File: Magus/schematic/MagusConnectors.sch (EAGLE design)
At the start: 7 parts

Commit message: Magus Rev01 board
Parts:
- renumbered C28 to C1, D3 to D1, D4 to D2, JP13 to JP2, JP3 to JP1
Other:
- note added: "Copyright 2017 Rebel Technology"
- note added: "Published under the GNU GPL"
- note removed: "Copyright Rebel Technology 2017"
- note removed: "Published under the GNU GPL v2"
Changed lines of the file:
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@@
 <part name="GND158" library="supply1" deviceset="GND" device=""/>
 <part name="GND159" library="supply1" deviceset="GND" device=""/>
-<part name="JP13" library="jumper" deviceset="JP1Q" device=""/>
+<part name="JP2" library="jumper" deviceset="JP1Q" device=""/>
 <part name="GND163" library="supply1" deviceset="GND" device=""/>
-<part name="C28" library="Rebel" deviceset="C-EU" device="C1206" value="10u"/>
+<part name="C1" library="Rebel" deviceset="C-EU" device="C1206" value="10u"/>
 <part name="P+13" library="supply1" deviceset="+5V" device=""/>
 <part name="X1" library="con-usb-3" deviceset="USB" device="-A-H"/>
 <part name="X3" library="con-usb-3" deviceset="USB" device="-B-H"/>
-<part name="JP3" library="pinhead" deviceset="PINHD-2X4" device=""/>
+<part name="JP1" library="pinhead" deviceset="PINHD-2X4" device=""/>
 <part name="GND26" library="supply1" deviceset="GND" device=""/>
-<part name="D3" library="diode" deviceset="BAT54S" device=""/>
-<part name="D4" library="diode" deviceset="BAT54S" device=""/>
+<part name="D1" library="diode" deviceset="BAT54S" device=""/>
+<part name="D2" library="diode" deviceset="BAT54S" device=""/>
 <part name="P+1" library="supply1" deviceset="+5V" device=""/>
 <part name="GND1" library="supply1" deviceset="GND" device=""/>
@@
 <plain>
 <text x="5.08" y="119.38" size="3.048" layer="97" font="vector">Magus Rev01</text>
-<text x="5.08" y="114.3" size="3.048" layer="97" font="vector">Copyright Rebel Technology 2017</text>
-<text x="5.08" y="109.22" size="3.048" layer="97" font="vector">Published under the GNU GPL v2</text>
+<text x="5.08" y="114.3" size="3.048" layer="97" font="vector">Copyright 2017 Rebel Technology</text>
+<text x="5.08" y="109.22" size="3.048" layer="97" font="vector">Published under the GNU GPL</text>
 </plain>
 <instances>
 <instance part="GND158" gate="1" x="53.34" y="78.74"/>
 <instance part="GND159" gate="1" x="53.34" y="35.56"/>
-<instance part="JP13" gate="A" x="43.18" y="45.72" smashed="yes" rot="R270">
+<instance part="JP2" gate="A" x="43.18" y="45.72" smashed="yes" rot="R270">
 <attribute name="NAME" x="40.64" y="43.18" size="1.778" layer="95"/>
 <attribute name="VALUE" x="38.1" y="41.275" size="1.778" layer="96"/>
 </instance>
 <instance part="GND163" gate="1" x="25.4" y="78.74"/>
-<instance part="C28" gate="G$1" x="25.4" y="88.9"/>
+<instance part="C1" gate="G$1" x="25.4" y="88.9"/>
 <instance part="P+13" gate="1" x="22.86" y="7.62" smashed="yes">
 <attribute name="VALUE" x="20.32" y="7.62" size="1.778" layer="96"/>
@@
 <instance part="X1" gate="G$1" x="58.42" y="91.44"/>
 <instance part="X3" gate="G$1" x="58.42" y="43.18"/>
-<instance part="JP3" gate="A" x="35.56" y="10.16"/>
+<instance part="JP1" gate="A" x="35.56" y="10.16"/>
 <instance part="GND26" gate="1" x="48.26" y="2.54"/>
-<instance part="D3" gate="G$1" x="20.32" y="93.98" rot="MR90"/>
-<instance part="D4" gate="G$1" x="5.08" y="45.72" rot="MR90"/>
+<instance part="D1" gate="G$1" x="20.32" y="93.98" rot="MR90"/>
+<instance part="D2" gate="G$1" x="5.08" y="45.72" rot="MR90"/>
 <instance part="P+1" gate="1" x="20.32" y="104.14"/>
 <instance part="GND1" gate="1" x="20.32" y="78.74"/>
@@
 <segment>
 <wire x1="50.8" y1="45.72" x2="55.88" y2="45.72" width="0.1524" layer="91"/>
-<pinref part="JP13" gate="A" pin="2"/>
+<pinref part="JP2" gate="A" pin="2"/>
 <pinref part="X3" gate="G$1" pin="VBUS"/>
 </segment>
@@
 <wire x1="33.02" y1="10.16" x2="5.08" y2="10.16" width="0.1524" layer="91"/>
 <label x="5.08" y="10.16" size="1.778" layer="95"/>
-<pinref part="JP3" gate="A" pin="5"/>
+<pinref part="JP1" gate="A" pin="5"/>
 </segment>
 </net>
@@
 <wire x1="33.02" y1="12.7" x2="5.08" y2="12.7" width="0.1524" layer="91"/>
 <label x="5.08" y="12.7" size="1.778" layer="95"/>
-<pinref part="JP3" gate="A" pin="3"/>
+<pinref part="JP1" gate="A" pin="3"/>
 </segment>
 </net>
 <net name="EXT_USB_D_VBUS" class="0">
 <segment>
-<pinref part="JP13" gate="A" pin="1"/>
+<pinref part="JP2" gate="A" pin="1"/>
 <wire x1="35.56" y1="45.72" x2="7.62" y2="45.72" width="0.1524" layer="91"/>
 <label x="10.16" y="45.72" size="1.778" layer="95"/>
-<pinref part="D4" gate="G$1" pin="C1A2"/>
+<pinref part="D2" gate="G$1" pin="C1A2"/>
 </segment>
 <segment>
 <wire x1="33.02" y1="15.24" x2="5.08" y2="15.24" width="0.1524" layer="91"/>
 <label x="5.08" y="15.24" size="1.778" layer="95"/>
-<pinref part="JP3" gate="A" pin="1"/>
+<pinref part="JP1" gate="A" pin="1"/>
 </segment>
 </net>
@@
 <wire x1="25.4" y1="93.98" x2="22.86" y2="93.98" width="0.1524" layer="91"/>
 <wire x1="25.4" y1="91.44" x2="25.4" y2="93.98" width="0.1524" layer="91"/>
-<pinref part="C28" gate="G$1" pin="1"/>
+<pinref part="C1" gate="G$1" pin="1"/>
 <pinref part="X1" gate="G$1" pin="VBUS"/>
-<pinref part="D3" gate="G$1" pin="C1A2"/>
+<pinref part="D1" gate="G$1" pin="C1A2"/>
 <junction x="25.4" y="93.98"/>
 </segment>
@@
 <wire x1="66.04" y1="15.24" x2="40.64" y2="15.24" width="0.1524" layer="91"/>
 <label x="45.72" y="15.24" size="1.778" layer="95"/>
-<pinref part="JP3" gate="A" pin="2"/>
+<pinref part="JP1" gate="A" pin="2"/>
 </segment>
 </net>
@@
 <wire x1="66.04" y1="12.7" x2="40.64" y2="12.7" width="0.1524" layer="91"/>
 <label x="45.72" y="12.7" size="1.778" layer="95"/>
-<pinref part="JP3" gate="A" pin="4"/>
+<pinref part="JP1" gate="A" pin="4"/>
 </segment>
 </net>
@@
 <wire x1="66.04" y1="10.16" x2="40.64" y2="10.16" width="0.1524" layer="91"/>
 <label x="45.72" y="10.16" size="1.778" layer="95"/>
-<pinref part="JP3" gate="A" pin="6"/>
+<pinref part="JP1" gate="A" pin="6"/>
 </segment>
 </net>
 <net name="+5V" class="0">
 <segment>
-<pinref part="D3" gate="G$1" pin="C2"/>
+<pinref part="D1" gate="G$1" pin="C2"/>
 <pinref part="P+1" gate="1" pin="+5V"/>
 <wire x1="20.32" y1="101.6" x2="20.32" y2="99.06" width="0.1524" layer="91"/>
 </segment>
 <segment>
-<pinref part="D4" gate="G$1" pin="C2"/>
+<pinref part="D2" gate="G$1" pin="C2"/>
 <pinref part="P+2" gate="1" pin="+5V"/>
 <wire x1="5.08" y1="53.34" x2="5.08" y2="50.8" width="0.1524" layer="91"/>
@@
 <pinref part="P+13" gate="1" pin="+5V"/>
 <wire x1="22.86" y1="2.54" x2="22.86" y2="5.08" width="0.1524" layer="91"/>
-<pinref part="JP3" gate="A" pin="7"/>
+<pinref part="JP1" gate="A" pin="7"/>
 <wire x1="33.02" y1="7.62" x2="25.4" y2="7.62" width="0.1524" layer="91"/>
 <wire x1="25.4" y1="7.62" x2="25.4" y2="2.54" width="0.1524" layer="91"/>
@@
 <net name="GND" class="0">
 <segment>
-<pinref part="D3" gate="G$1" pin="A1"/>
+<pinref part="D1" gate="G$1" pin="A1"/>
 <pinref part="GND1" gate="1" pin="GND"/>
 <wire x1="20.32" y1="81.28" x2="20.32" y2="88.9" width="0.1524" layer="91"/>
 </segment>
 <segment>
-<pinref part="D4" gate="G$1" pin="A1"/>
+<pinref part="D2" gate="G$1" pin="A1"/>
 <pinref part="GND2" gate="1" pin="GND"/>
 <wire x1="5.08" y1="38.1" x2="5.08" y2="40.64" width="0.1524" layer="91"/>
@@
 <pinref part="GND163" gate="1" pin="GND"/>
 <wire x1="25.4" y1="81.28" x2="25.4" y2="83.82" width="0.1524" layer="91"/>
-<pinref part="C28" gate="G$1" pin="2"/>
+<pinref part="C1" gate="G$1" pin="2"/>
 </segment>
 <segment>
-<pinref part="JP3" gate="A" pin="8"/>
+<pinref part="JP1" gate="A" pin="8"/>
 <pinref part="GND26" gate="1" pin="GND"/>
 <wire x1="40.64" y1="7.62" x2="48.26" y2="7.62" width="0.1524" layer="91"/>

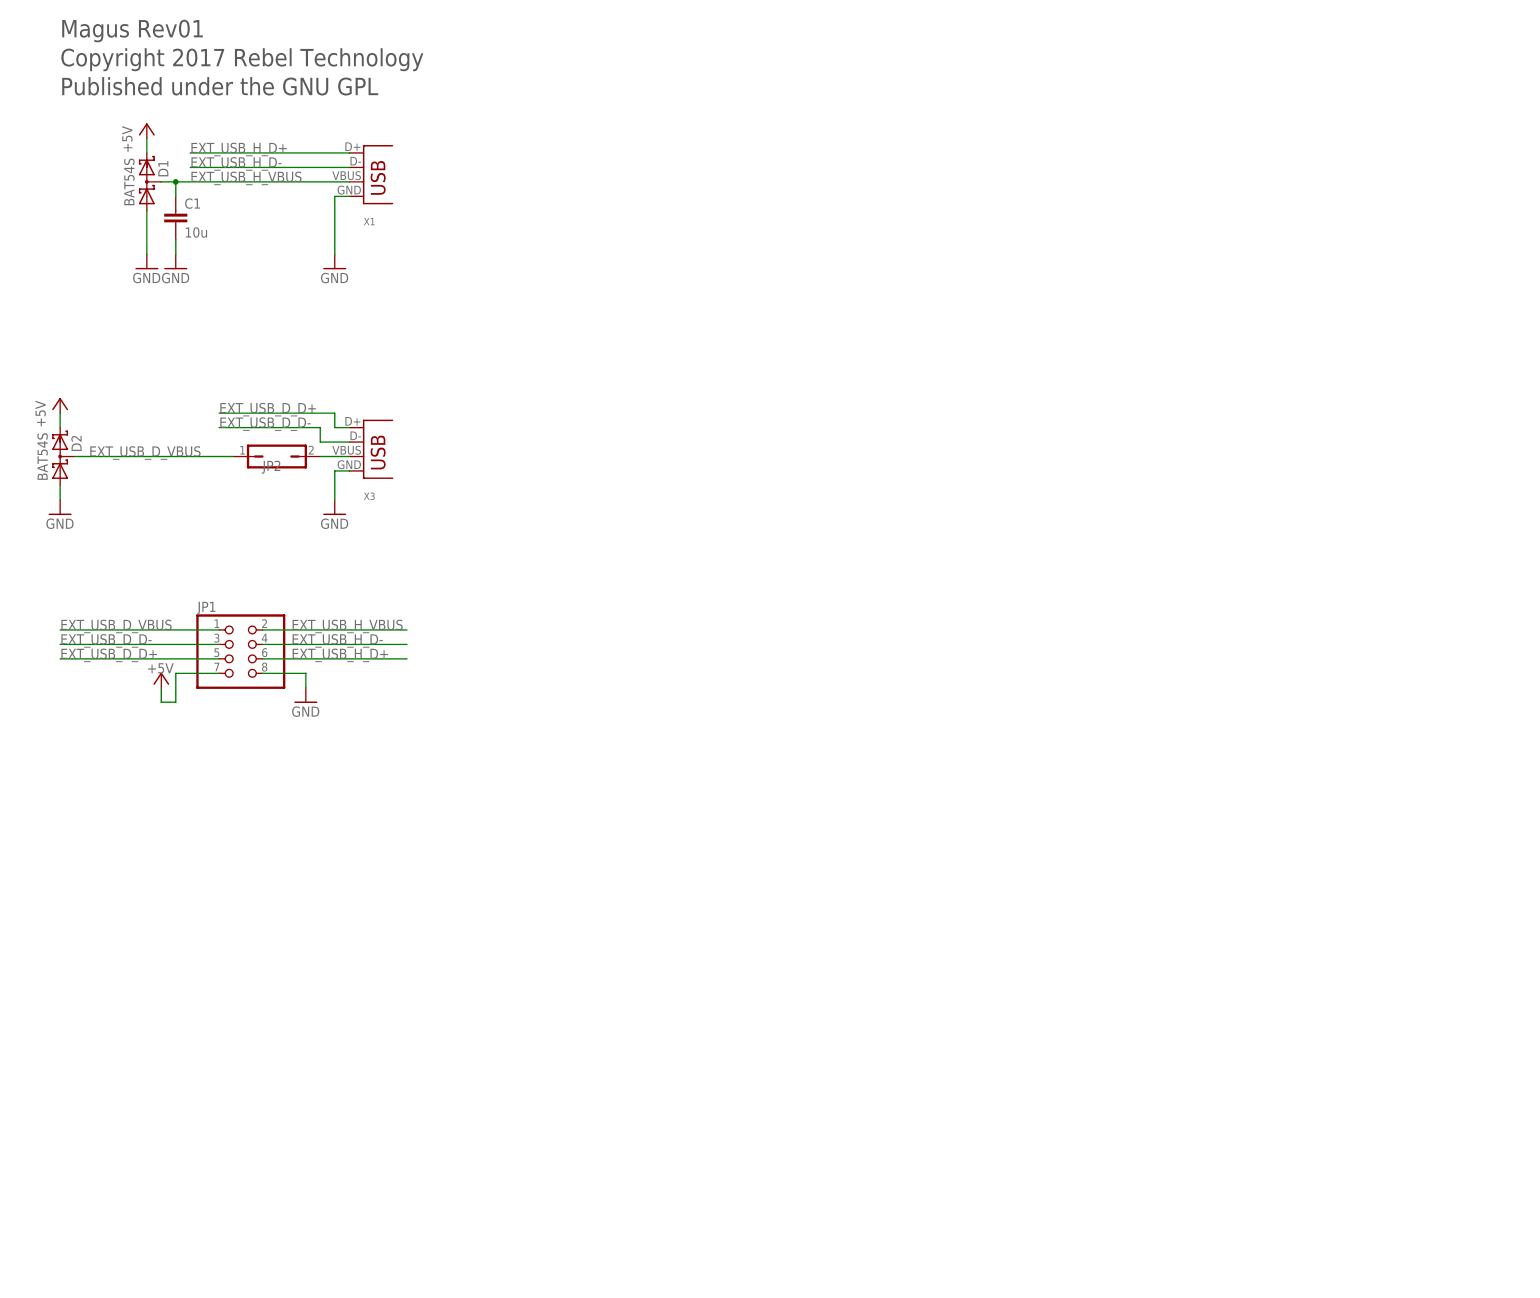
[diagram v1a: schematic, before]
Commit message: second revison of Magus connector board draft completed
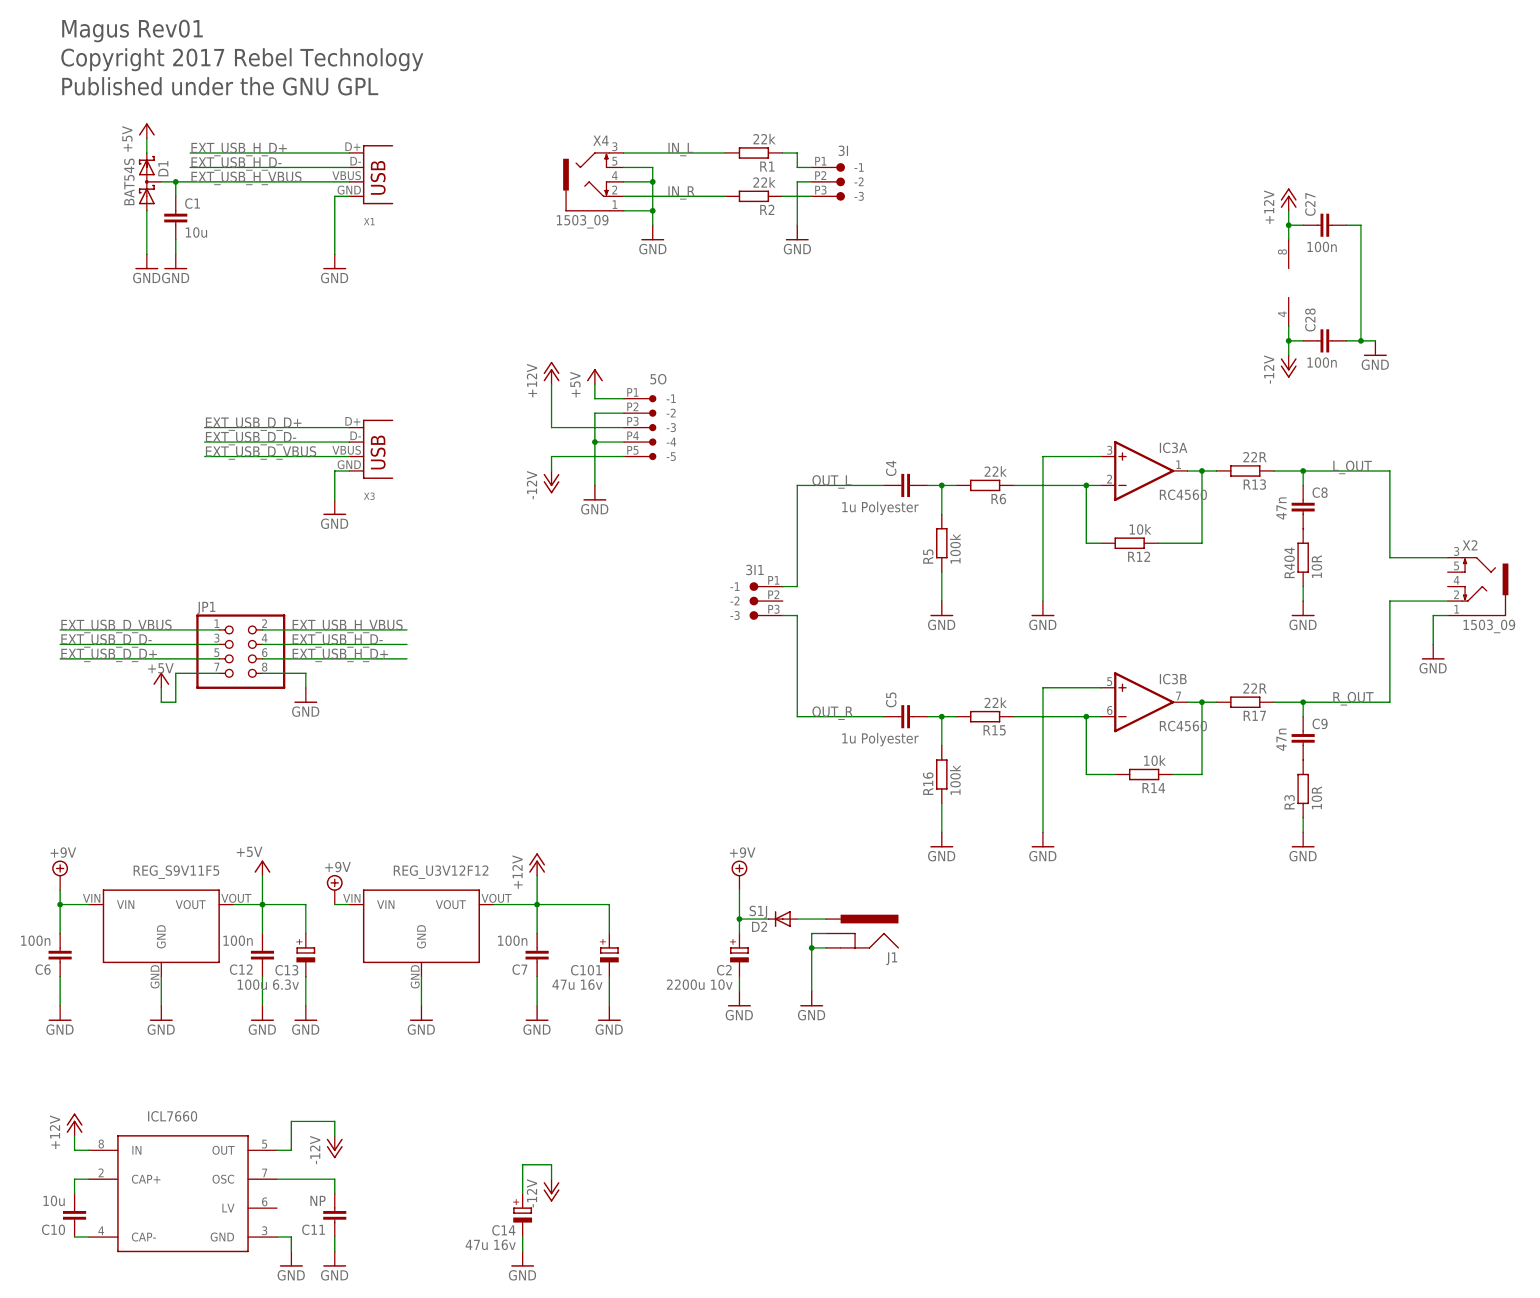
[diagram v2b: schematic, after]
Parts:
- removed JP2: (no value), jumper:JP1Q
- added 3I, 3I1: CON-JST_PH_3W, Rebel:CON-JST_PH_3W
- added 5O: CON-JST_PH_5W, Rebel:CON-JST_PH_5W
- added C10: 10u, rcl:C-EUC1206
- added C101, C14: 47u 16v, Rebel:CPOL-EUB
- added C11: NP, rcl:C-EUC0603
- added C12, C6, C7: 100n, rcl:C-EUC0603
- added C13: 100u 6.3v, Rebel:CPOL-EUB
- added C2: 2200u 10v, Rebel:CPOL-EUD
- added C27, C28: 100n, Rebel:C-EUC0603
- added C4, C5: 1u Polyester, Rebel:C-EUC1210
- added C8, C9: 47n, Rebel:C-EUC0603
- added IC3: RC4560, linear:NE5532D
- added J1: POWER_JACKPTH, SparkFun:POWER_JACKPTH
- added R1, R15, R2, R6: 22k, resistor:R-EU_R0603
- added R12, R14: 10k, resistor:R-EU_R0603
- added R13, R17: 22R, resistor:R-EU_R0603
- added R16, R5: 100k, resistor:R-EU_R0603
- added R3, R404: 10R, resistor:R-EU_R0603
- added U1: REG_S9V11F5, Rebel:REG_S9V11F5
- added U2: REG_U3V12F12, Rebel:REG_S9V11F5
- added U3: ICL7660, Rebel:ICL7660
- added X2, X4: 1503_09, con-lumberg:1503_09
- D2: value BAT54S -> S1J; device diode:BAT54S -> SparkFun:DIODESMA
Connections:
- removed net N$50: JP2.2, X3.VBUS
- new net +12V: 5O.-3, C101.+, C27.1, C7.2, IC3P.V+, U2.VOUT, U3.IN
- new net +9V: C2.+, C6.2, D2.C, U1.VIN, U2.VIN
- new net -12V: 5O.-5, C14.+, C28.1, IC3P.V-, U3.OUT
- new net IN_L: R1.2, X4.3
- new net IN_R: R2.2, X4.2
- new net L_OUT: C8.1, R13.1, X2.3
- new net N$1: IC3B.-IN, R14.2, R15.1
- new net N$10: C10.1, U3.CAP-
- new net N$11: C10.2, U3.CAP+
- new net N$12: C9.2, R3.2
- new net N$13: C11.2, U3.OSC
- new net N$19: IC3A.OUT, R12.1, R13.2
- new net N$2: IC3B.OUT, R14.1, R17.2
- new net N$21: C8.2, R404.2
- new net N$3: IC3A.-IN, R12.2, R6.1
- new net N$4: C5.2, R15.2, R16.2
- new net N$5: 3I.-3, R2.1
- new net N$6: 3I.-1, R1.1
- new net N$8: C4.2, R5.2, R6.2
- new net N$9: D2.A, J1.PWR
- new net OUT_L: 3I1.-1, C4.1
- new net OUT_R: 3I1.-3, C5.1
- new net R_OUT: C9.1, R17.1, X2.2
- net +5V: now also 5O.-1, C12.2, C13.+, U1.VOUT; no longer D2.C2
- net EXT_USB_D_VBUS: now also X3.VBUS; no longer D2.C1A2, JP2.1
- net GND: now also 3I.-2, 5O.-2, 5O.-4, C101.-, C11.1, C12.1, C13.-, C14.-, C2.-, C27.2, C28.2, C6.1, C7.1, IC3A.+IN, IC3B.+IN, J1.GND, J1.GNDBREAK, R16.1, R3.1, R404.1, R5.1, U1.GND, U2.GND, U3.GND, X2.1, X4.1, X4.4, X4.5; no longer D2.A1
